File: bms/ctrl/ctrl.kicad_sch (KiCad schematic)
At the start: 1 part

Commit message: BMS stuff update
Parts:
- removed Q?: Q_NMOS_GSD, symbol Device:Q_NMOS_GSD
- added C (x2): CP_1µ_100V_0805, Resistor_SMD:R_0805_2012Metric, symbol localparts:CP_10µ_100V_1210
- added C (x3): CP_100n_50V_0603, Capacitor_SMD:C_0603_1608Metric, symbol localparts:CP_100n_50V_0603
- added C: CP_330µ_100V_1210, localstuff:CP_Elec_19x19, symbol localparts:CP_330µ_100V_1210
- added C: CP_10µ_16V_0603, Capacitor_SMD:C_0603_1608Metric, symbol localparts:CP_10µ_16V_0603
- added D (x4): 1N4148, Diode_THT:D_DO-35_SOD27_P7.62mm_Horizontal, symbol Diode:1N4148
- added D: D_Zener_3V3, localstuff:SOD80, symbol localparts:D_Zener_3V3
- added D: D_Schottky, symbol localstuff:D_Schottky
- added D: D_TVS_70V, localstuff:SOD-123FL, symbol localparts:D_TVS_70V
- added F: Polyfuse 100V, Diode_SMD:D_SMA, symbol localparts:Polyfuse 100V
- added J: Conn_01x06, symbol Connector_Generic:Conn_01x06
- added J (x4): Conn_01x02_Female, symbol Connector:Conn_01x02_Female
- added J (x2): Conn_01x04, symbol Connector_Generic:Conn_01x04
- added J: Conn_LEM_5, Connector_JST:JST_PH_B4B-PH-K_1x04_P2.00mm_Vertical, symbol localstuff:Conn_LEM_5
- added J: Conn_01x02_Female, symbol Connector:Conn_01x02_Male
- added J: Conn_LEM_3, Connector_JST:JST_PH_B5B-PH-K_1x05_P2.00mm_Vertical, symbol localstuff:Conn_LEM_3
- added J: Conn_01x03, symbol Connector_Generic:Conn_01x03
- added JP: Jumper_2_Open, symbol Jumper:Jumper_2_Open
- added Q (x2): ST23690, Package_DFN_QFN:AO_DFN-8-1EP_5.55x5.2mm_P1.27mm_EP4.12x4.6mm, symbol Transistor_FET:BSS83P
- added Q (x4): 2N7002, Package_TO_SOT_SMD:SOT-23, symbol localparts:Q_NMOS_20V_4A_lowVth
- added R: R_120_0603, Resistor_SMD:R_0603_1608Metric, symbol localparts:R_120_0603
- added R: R_10k_0603, Resistor_SMD:R_0603_1608Metric, symbol localparts:R_10k_0603
- added R (x6): R_1M_0603, Resistor_SMD:R_0603_1608Metric, symbol localparts:R_1M_0603
- added R: R_36k_0603_1, Resistor_SMD:R_0603_1608Metric, symbol localparts:R_36k_0603_1
- added R: R_750k_0603, Resistor_SMD:R_0603_1608Metric, symbol localparts:R_750k_0603
- added TP: TestPoint, symbol Connector:TestPoint
- added U: SN65HVD1050D, Package_SO:SOIC-8_3.9x4.9mm_P1.27mm, symbol Interface_CAN_LIN:SN65HVD1050D
- added U (x6): (no value), symbol Jumper:SolderJumper_3_Bridged12
- added U: STH05_12, localstuff:STH05, symbol localstuff:STH05_12
- added U: (no value), symbol Jumper:SolderJumper_2_Open
- added U: (no value), symbol ControllerCircuit:SN65HVD75DR
- added U (x2): (no value), symbol Connector:Conn_01x02_Male
- added U: (no value), symbol localparts:R_2k2_0603
- added U: (no value), symbol Device:R
- added U: (no value), symbol Connector:Conn_01x04_Female
- added U: Pico, RPi_Pico:RPi_Pico_SMD_TH, symbol pico:Pico
- added U: (no value), symbol localparts:R_220_0603
- added U: (no value), symbol localparts:CP_100n_50V_0603
- added U: VOS618A, Package_SO:SOP-4_4.4x2.6mm_P1.27mm, symbol localparts:VOS618A
- added U: STH05_5V, localstuff:STH05, symbol localstuff:STH05_5V
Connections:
- net +5V: now also D.2 (A), J.1 (+), J.3 (Pin_3), Q.3 (D), R.1, U.1 (A), U.1 (Pin_1), U.5 (+Vout)
- net GND: now also C.2, C.2, C.2, C.2, C.2, C.2, C.2, D.2 (A), D.2 (A), D.2 (A), J.1 (Pin_1), J.2 (GND), J.2 (Pin_2), J.2 (Pin_2), J.2 (Pin_2), J.3 (Pin_3), J.4 (GND), J.4 (Pin_4), J.6 (Pin_6), Q.2 (S), Q.2 (S), Q.2 (S), Q.2 (S), R.2, R.2, R.2, R.2, R.2, U.1 (A), U.1 (A), U.13 (GND), U.18 (GND), U.2, U.2 (GND), U.23 (GND), U.28 (GND), U.3 (B), U.3 (GND), U.33 (AGND), U.38 (GND), U.4 (Pin_4), U.5 (GND), U.7 (GND), U.7 (GND), U.8 (GND), U.9 (GND), U.9 (GND)
- net VBAT: now also C.1, C.1, C.1, D.1 (K), F.2, R.1, U.1 (+Vin), U.1 (+Vin)
- new net: C.1, U.2 (C), U.3 (VCC)
- new net: J.2 (Pin_2), JP.2 (B), U.6 (CANL)
- new net: J.1 (Pin_1), R.1, U.7 (CANH)
- new net: JP.1 (A), R.2
- new net: F.1, J.1 (Pin_1)
- new net: D.2 (A), J.2 (Pin_2), Q.3 (D) (x2)
- new net: Q.1 (G), Q.3 (D), R.2 (x2)
- new net: D.2 (A), Q.2 (S)
- new net: U.1 (A), U.2 (Pin_2), U.7 (B)
- new net: U.1, U.2 (B)
- new net: U.1, U.1 (A), U.3 (B)
- new net: U.1, U.2 (C)
- new net: D.1 (K), D.1 (K), J.1 (Pin_1), Q.2 (S)
- new net: U.1 (Pin_1), U.2 (C)
- new net: U.2, U.3 (Pin_3), U.6 (A)
- new net: U.1 (Pin_1), U.3
- new net: U.2 (Pin_2), U.4
- new net: U.2, U.2 (C) (x2)
- new net: D.1 (K), U.39 (VSYS)
- new net: U.2 (C), U.2 (Pin_2)
- new net +12V: D.1 (K), D.1 (K), J.1 (Pin_1), J.1 (Pin_1), J.4 (Pin_4), Q.3 (D), R.1, U.5 (+Vout)
- new net +3V3: J.1 (+), J.1 (Pin_1), J.1 (Pin_1), J.2 (Pin_2), R.1, U.1, U.1 (A), U.3 (B), U.3 (B), U.3 (B), U.36 (3V3), U.8 (VCC)
- new net ADC_BAT_I: C.1, D.1 (K), J.3 (Out), J.3 (Out), U.32 (GPIO27_ADC1)
- new net ADC_BAT_U: C.1, R.1, R.2, TP.1, U.31 (GPIO26_ADC0)
- new net ADC_REF_I: C.1, J.2 (Ref), J.4 (Ref), U.34 (GPIO28_ADC2)
- new net CAN_RX: U.10 (GPIO7), U.4 (RXD)
- new net CAN_S: U.14 (GPIO10), U.8 (S)
- new net CAN_TX: U.1 (TXD), U.9 (GPIO6)
- new net I2C0_SCL: J.3 (Pin_3), U.17 (GPIO13)
- new net I2C0_SDA: J.2 (Pin_2), U.16 (GPIO12)
- new net IO1: J.2 (Pin_2), U.27 (GPIO21)
- new net IO2: J.3 (Pin_3), U.26 (GPIO20)
- new net IO3: J.4 (Pin_4), U.25 (GPIO19)
- new net IO4: J.5 (Pin_5), U.24 (GPIO18)
- new net RELAY1: Q.1 (G), R.1, U.4 (GPIO2)
- new net RELAY2: Q.1 (G), R.1, U.5 (GPIO3)
- new net RELAY3H: Q.1 (G), R.1, U.7 (GPIO5)
- new net RELAY3L: Q.1 (G), R.1, U.6 (GPIO4)
- new net RESET: J.1 (Pin_1), R.2, U.30 (RUN)
- new net RS485_ENA: U.15 (GPIO11), U.2 (RE), U.3 (DE)
- new net RS485_RX: U.1 (R), U.12 (GPIO9)
- new net RS485_TX: U.11 (GPIO8), U.4 (D)
- new net RX_BAT: U.1, U.1 (A), U.2 (GPIO1), U.3 (B)
- new net TX_BAT: U.1 (GPIO0), U.2
- no-connect marks 0 -> 1
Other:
- note added: "12V actuate / 5V hold relay"
- note added: "24V: R8 220k, R9 22k 12V: R8 160k"
- note added: "48V battery monitor"
- note added: "CAN transceiver"
- note added: "Connect 1-2 for diyBMS active-high Connect 2-3 for MoaT active-low"
- note added: "I2C"
- note added: "Pico module"
- note added: "Power supply 12V 0.5A 5V 0.5A"
- note added: "RESET button"
- note added: "RS485"
- note added: "Two 12V / open collector outputs"
- note added: "U1 and U2 share capacitor and TVS"
- note added: "aux I/O"

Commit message: minor fixup
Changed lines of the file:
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@@
     (in_bom yes) (on_board yes)
     (default_instance (reference "U") (unit 1) (value "") (footprint ""))
-    (property "Reference" "U" (id 0) (at 135.001 171.577 0)
+    (property "Reference" "U" (id 0) (at 135.89 173.99 0)
       (effects (font (size 1.27 1.27)))
     )

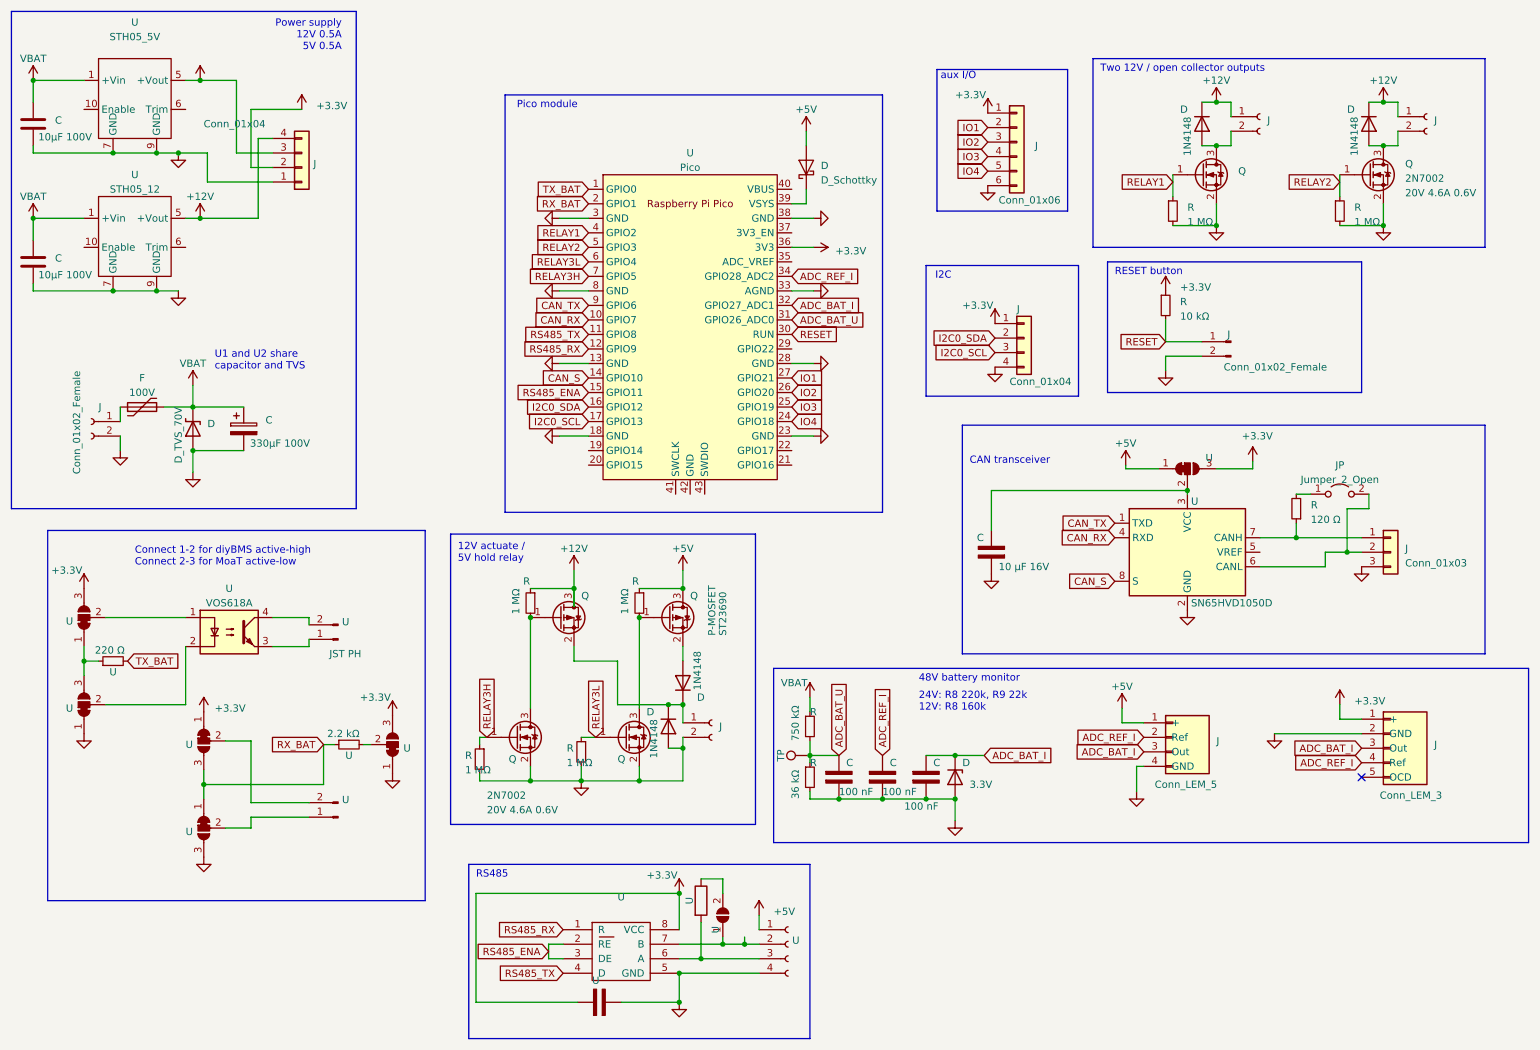
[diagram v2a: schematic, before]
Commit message: Added two more config jumpers
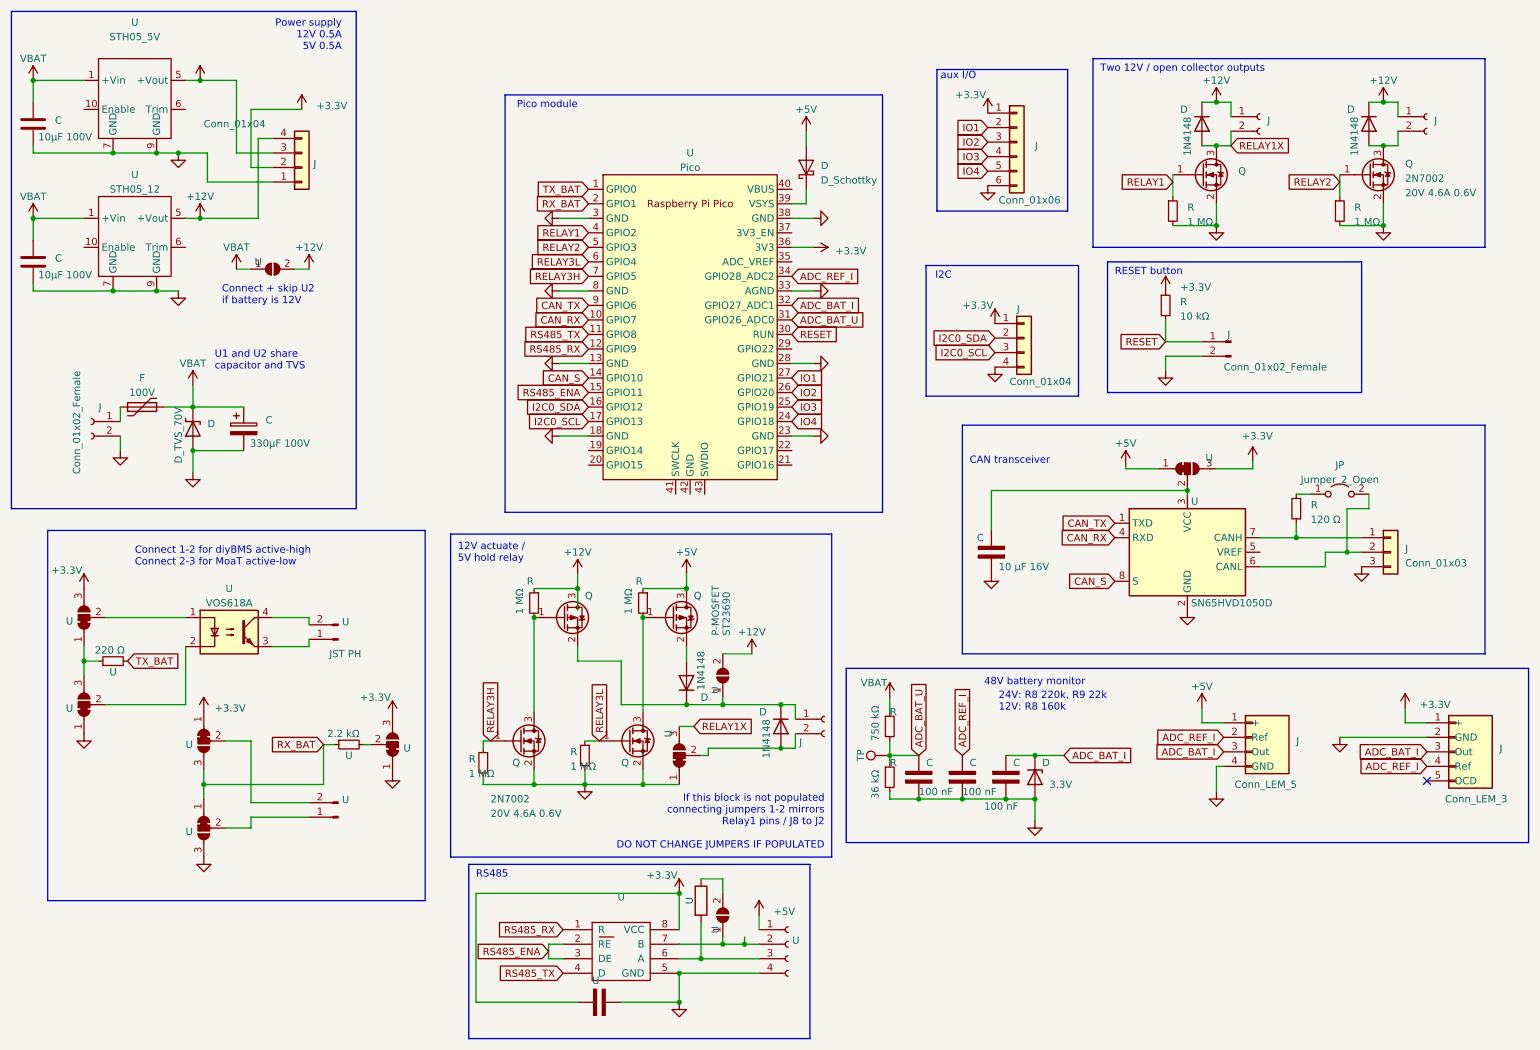
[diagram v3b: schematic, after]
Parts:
- added U: (no value), symbol Jumper:SolderJumper_3_Bridged12
- added U (x2): (no value), symbol Jumper:SolderJumper_2_Open
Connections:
- net +12V: now also U.2 (B), U.2 (B)
- net GND: now also U.1 (A); no longer D.2 (A), J.2 (Pin_2)
- net VBAT: now also U.1 (A)
- net RELAY1X: now reaches D.2 (A), J.2 (Pin_2), Q.3 (D)
- net RELAY1X: now also U.3 (B)
- net at D.1 (K), D.1 (K), J.1 (Pin_1)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: now also U.1 (A)
- new net: D.2 (A), J.2 (Pin_2), U.2 (C)
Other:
- note added: "Connect + skip U2 if battery is 12V"
- note added: "If this block is not populated connecting jumpers 1-2 mirrors Relay1 pins / J8 to J2 DO NOT CHANGE JUMPERS IF POPULATED"
- moved on the sheet: C, D, J, Q, R, TP

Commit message: BMS hardware (prev)
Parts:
- removed C: CP_330µ_100V_1210, localstuff:CP_Elec_19x19, symbol localparts:CP_330µ_100V_1210
- removed JP: Jumper_2_Open, symbol Jumper:Jumper_2_Open
- removed U: (no value), symbol Jumper:SolderJumper_3_Bridged12
- removed U: (no value), symbol Jumper:SolderJumper_2_Open
- added D: LED_green, LED_SMD:LED_0805_2012Metric, symbol localparts:LED_green
- added D: LED_red, LED_SMD:LED_0805_2012Metric, symbol localparts:LED_red
- added R: R_510_0603, Resistor_SMD:R_0603_1608Metric, symbol localparts:R_510_0603
- added R (x2): R_750k_0603, Resistor_SMD:R_0603_1608Metric, symbol localparts:R_750k_0603
- added R: R_560_0603, Resistor_SMD:R_0603_1608Metric, symbol localparts:R_560_0603
- added U (x3): (no value), symbol Jumper:SolderJumper_2_Open
- D: symbol Diode:1N4148 -> localstuff:D_Schottky; now left out of the parts list
- D, J, Q, R: now left out of the parts list
- J: symbol Connector:Conn_01x02_Female -> Connector:Conn_01x02_Male
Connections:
- net +12V: now also J.1 (Pin_1); no longer J.4 (Pin_4)
- net +3V3: now also J.3 (Pin_3), R.1, R.2; no longer J.2 (Pin_2)
- net +5V: now also J.2 (Pin_2), U.4 (Pin_4); no longer J.3 (Pin_3), U.1 (Pin_1)
- net ADC_BAT_U: now also U.2 (B), U.2 (B)
- net GND: now also D.2 (A), J.1 (Pin_1), J.1 (Pin_1), J.4 (Pin_4), U.1 (Pin_1); no longer J.1 (Pin_1), J.2 (Pin_2), U.4 (Pin_4)
- net VBAT: now also R.1, R.1
- net at J.2 (Pin_2), U.6 (CANL): now also U.1 (A)
- net at R.2: now also U.2 (B)
- net at J.2 (Pin_2): now also D.1 (K), D.1 (K), Q.2 (S); no longer D.2 (A)
- net at F.1: now also J.2 (Pin_2); no longer J.1 (Pin_1)
- net at U.1 (A), U.7 (B): now also U.3 (Pin_3); no longer U.2 (Pin_2)
- net at U.2, U.6 (A): now also U.2 (Pin_2); no longer U.3 (Pin_3)
- net LED_RED: now reaches U.21 (GPIO16)
- net LED_RED: now also D.1 (K)
- net LED_GREEN: now reaches U.22 (GPIO17)
- net LED_GREEN: now also D.1 (K)
- net RELAY1X: no longer names the net of D.2 (A), J.2 (Pin_2), Q.3 (D)
- new net: R.2, U.1 (A) (x2)
- new net: D.2 (A), R.1
- new net: D.2 (A), R.2
- no-connect marks 1 -> 10
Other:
- note added: "12V"
- note added: "12V/24V/48V battery monitor"
- note added: "24V"
- note added: "Blinkenlights"
- note added: "This block is excluded: most relays don't reliably hold at 5V"
- note removed: "24V: R8 220k, R9 22k 12V: R8 160k"
- note removed: "48V battery monitor"
- note removed: "If this block is not populated connecting jumpers 1-2 mirrors Relay1 pins / J8 to J2 DO NOT CHANGE JUMPERS IF POPULATED"
- moved on the sheet: C, D, J, R, U

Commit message: Old check-in: ctrl
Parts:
- removed C: CP_1µ_100V_0805, Resistor_SMD:R_0805_2012Metric, symbol localparts:CP_10µ_100V_1210
- removed C: CP_100n_50V_0603, Capacitor_SMD:C_0603_1608Metric, symbol localparts:CP_100n_50V_0603
- removed C: CP_10µ_16V_0603, Capacitor_SMD:C_0603_1608Metric, symbol localparts:CP_10µ_16V_0603
- removed D: LED_green, LED_SMD:LED_0805_2012Metric, symbol localparts:LED_green
- removed D: D_Zener_3V3, localstuff:SOD80, symbol localparts:D_Zener_3V3
- removed D: 1N4148, Diode_THT:D_DO-35_SOD27_P7.62mm_Horizontal, symbol localstuff:D_Schottky
- removed D (x2): 1N4148, Diode_THT:D_DO-35_SOD27_P7.62mm_Horizontal, symbol Diode:1N4148
- removed D: D_Schottky, symbol localstuff:D_Schottky
- removed D: LED_red, LED_SMD:LED_0805_2012Metric, symbol localparts:LED_red
- removed J: Conn_01x06, symbol Connector_Generic:Conn_01x06
- removed J: Conn_01x02_Female, symbol Connector:Conn_01x02_Female
- removed J (x2): Conn_01x02_Female, symbol Connector:Conn_01x02_Male
- removed J: Conn_01x03, symbol Connector_Generic:Conn_01x03
- removed Q (x2): ST23690, Package_DFN_QFN:AO_DFN-8-1EP_5.55x5.2mm_P1.27mm_EP4.12x4.6mm, symbol Transistor_FET:BSS83P
- removed Q (x2): 2N7002, Package_TO_SOT_SMD:SOT-23, symbol localparts:Q_NMOS_20V_4A_lowVth
- removed R: R_120_0603, Resistor_SMD:R_0603_1608Metric, symbol localparts:R_120_0603
- removed R: R_10k_0603, Resistor_SMD:R_0603_1608Metric, symbol localparts:R_10k_0603
- removed R: R_510_0603, Resistor_SMD:R_0603_1608Metric, symbol localparts:R_510_0603
- removed R (x4): R_1M_0603, Resistor_SMD:R_0603_1608Metric, symbol localparts:R_1M_0603
- removed R: R_36k_0603_1, Resistor_SMD:R_0603_1608Metric, symbol localparts:R_36k_0603_1
- removed R (x3): R_750k_0603, Resistor_SMD:R_0603_1608Metric, symbol localparts:R_750k_0603
- removed R: R_560_0603, Resistor_SMD:R_0603_1608Metric, symbol localparts:R_560_0603
- removed TP: TestPoint, symbol Connector:TestPoint
- removed U: SN65HVD1050D, Package_SO:SOIC-8_3.9x4.9mm_P1.27mm, symbol Interface_CAN_LIN:SN65HVD1050D
- removed U (x6): (no value), symbol Jumper:SolderJumper_3_Bridged12
- removed U (x4): (no value), symbol Jumper:SolderJumper_2_Open
- removed U: STH05_12, localstuff:STH05, symbol localstuff:STH05_12
- removed U: (no value), symbol ControllerCircuit:SN65HVD75DR
- removed U (x2): (no value), symbol Connector:Conn_01x02_Male
- removed U: (no value), symbol localparts:R_2k2_0603
- removed U: (no value), symbol Device:R
- removed U: (no value), symbol Connector:Conn_01x04_Female
- removed U: Pico, RPi_Pico:RPi_Pico_SMD_TH, symbol pico:Pico
- removed U: (no value), symbol localparts:R_220_0603
- removed U: (no value), symbol localparts:CP_100n_50V_0603
- removed U: VOS618A, Package_SO:SOP-4_4.4x2.6mm_P1.27mm, symbol localparts:VOS618A
- removed U: STH05_5V, localstuff:STH05, symbol localstuff:STH05_5V
- added C3: CP_22m_16V, Capacitor_THT:CP_Radial_D22.0mm_P10.00mm_SnapIn, symbol localparts:CP_22m_16V
- added R16: R_22_0603, Resistor_SMD:R_0603_1608Metric, symbol localparts:R_22_0603
- added R3, R4: R_5k1_0603, Resistor_SMD:R_0603_1608Metric, symbol localparts:R_5k1_0603
- added U4: TSR_1-48150WI, localstuff:TSR_1-48150WI, symbol localstuff:TSR_1-48150WI
- added U7: tiny2040, localstuff:tiny2040, symbol localstuff:tiny2040
- C2: renamed from C; footprint Resistor_SMD:R_0805_2012Metric -> Resistor_SMD:R_1210_3225Metric
- D5: renamed from D; footprint Diode_THT:D_DO-35_SOD27_P7.62mm_Horizontal -> Diode_SMD:D_SOD-123
- F1: renamed from F; value Polyfuse 100V -> Fuse; footprint Diode_SMD:D_SMA -> Fuse:Fuseholder_Cylinder-5x20mm_Stelvio-Kontek_PTF78_Horizontal_Open; Display 100V -> 200mA; Farnell 3945785 -> (none)
- J1, J8: renamed from J; footprint (none) -> localstuff:Conn_P5.0mm_2_Lumberg
- J12, J5: renamed from J; footprint (none) -> Connector_PinHeader_2.54mm:PinHeader_1x04_P2.54mm_Vertical
- JP11: renamed from U; value (none) -> Bat12V; footprint (none) -> Jumper:SolderJumper-2_P1.3mm_Open_RoundedPad1.0x1.5mm
- Q5, Q6: renamed from Q; value 2N7002 -> DMN2058U-7
- renumbered C to C6, C to C7, D to D1, J to J10, J to J6, R to R11, R to R13
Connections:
- net +12V: now also J12.4 (Pin_4), C3.1, U4.3 (+VOUT); no longer J12.1 (Pin_1)
- net +3V3: now also J12.2 (Pin_2), J5.4 (Pin_4), R3.1, R4.1, U7.3 (3V3); no longer J12.3 (Pin_3), J5.1 (Pin_1)
- net +5V: now also J12.3 (Pin_3), U7.1 (VBUS); no longer J12.2 (Pin_2)
- net GND: now also J12.1 (Pin_1), J5.1 (Pin_1), U4.2 (GND), U7.2 (GND), U7.8 (GND); no longer J12.4 (Pin_4), J5.4 (Pin_4)
- net I2C0_SCL: now also J5.2 (Pin_2), R3.2, U7.6 (GP27); no longer J5.3 (Pin_3)
- net I2C0_SDA: now also J5.3 (Pin_3), R4.2, U7.7 (GP26); no longer J5.2 (Pin_2)
- net RELAY1: now also U7.14 (GP2)
- net RELAY2: now also U7.13 (GP3)
- net RX_BAT: now also U7.15 (GP1)
- net TX_BAT: now also U7.16 (GP0)
- net VBAT: now also U4.1 (+VIN)
- net at Q6.3 (D): now also R16.1
- new net: U4.4 (CASE_PIN), U4.5 (CASE_PIN)
- new net: C3.2, R16.2
- new net SCK: U7.10 (GP6)
- new net SCSn: U7.11 (GP5)
- new net SRX: U7.12 (GP4)
- new net STX: U7.9 (GP7)
- no-connect marks 10 -> 1
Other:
- note added: "Connect + skip U4 if battery is 12V"
- note added: "Open collector output"
- note added: "Power supply 12V 0.5A"
- note removed: "12V"
- note removed: "12V actuate / 5V hold relay"
- note removed: "12V/24V/48V battery monitor"
- note removed: "24V"
- note removed: "Blinkenlights"
- note removed: "CAN transceiver"
- note removed: "Connect + skip U2 if battery is 12V"
- note removed: "Connect 1-2 for diyBMS active-high Connect 2-3 for MoaT active-low"
- note removed: "Power supply 12V 0.5A 5V 0.5A"
- note removed: "RESET button"
- note removed: "RS485"
- note removed: "This block is excluded: most relays don't reliably hold at 5V"
- note removed: "Two 12V / open collector outputs"
- note removed: "U1 and U2 share capacitor and TVS"
- note removed: "aux I/O"
- moved on the sheet: J5
